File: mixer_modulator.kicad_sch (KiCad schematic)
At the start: 8 parts, among them U4 SA612, U5 SA612, U6 SA612, U7 SA612

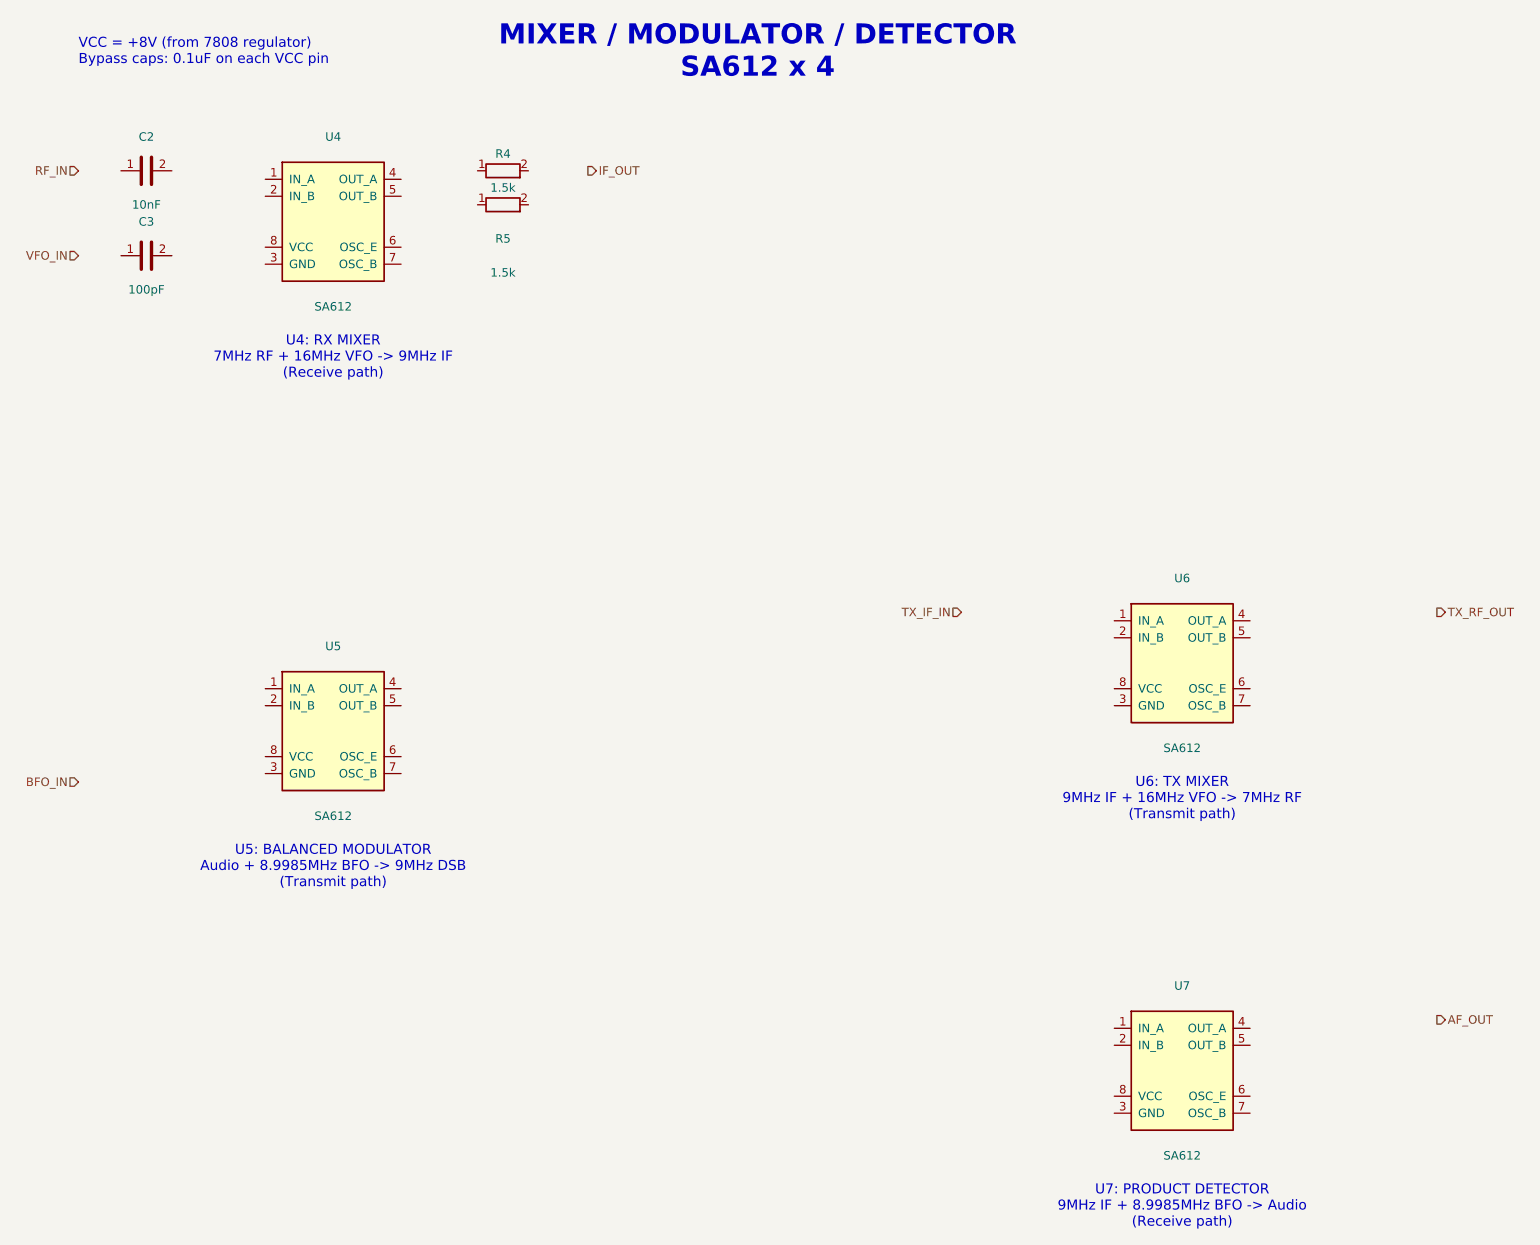
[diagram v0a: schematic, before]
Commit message: Add initial PCB layout with complete component placement
- Create 2-layer PCB (200x100mm) based on KiCad schematic import
- Place all components including Arduino Nano, Si5351, SA612 mixers, SSD1306 OLED
- Position audio amplifier (LM386), voltage regulators (7805/7808), crystal filters
- Add discrete components: resistors, capacitors, inductors, diodes, transistors
- Include connectors for power (DC jack), antenna, speaker, and microphone
- Update .gitignore to exclude fp-info-cache and backup directories
- Update schematic symbols for all circuit blocks (audio, BPF/LPF, control, IF filter, mixer/modulator, power amp, power supply)
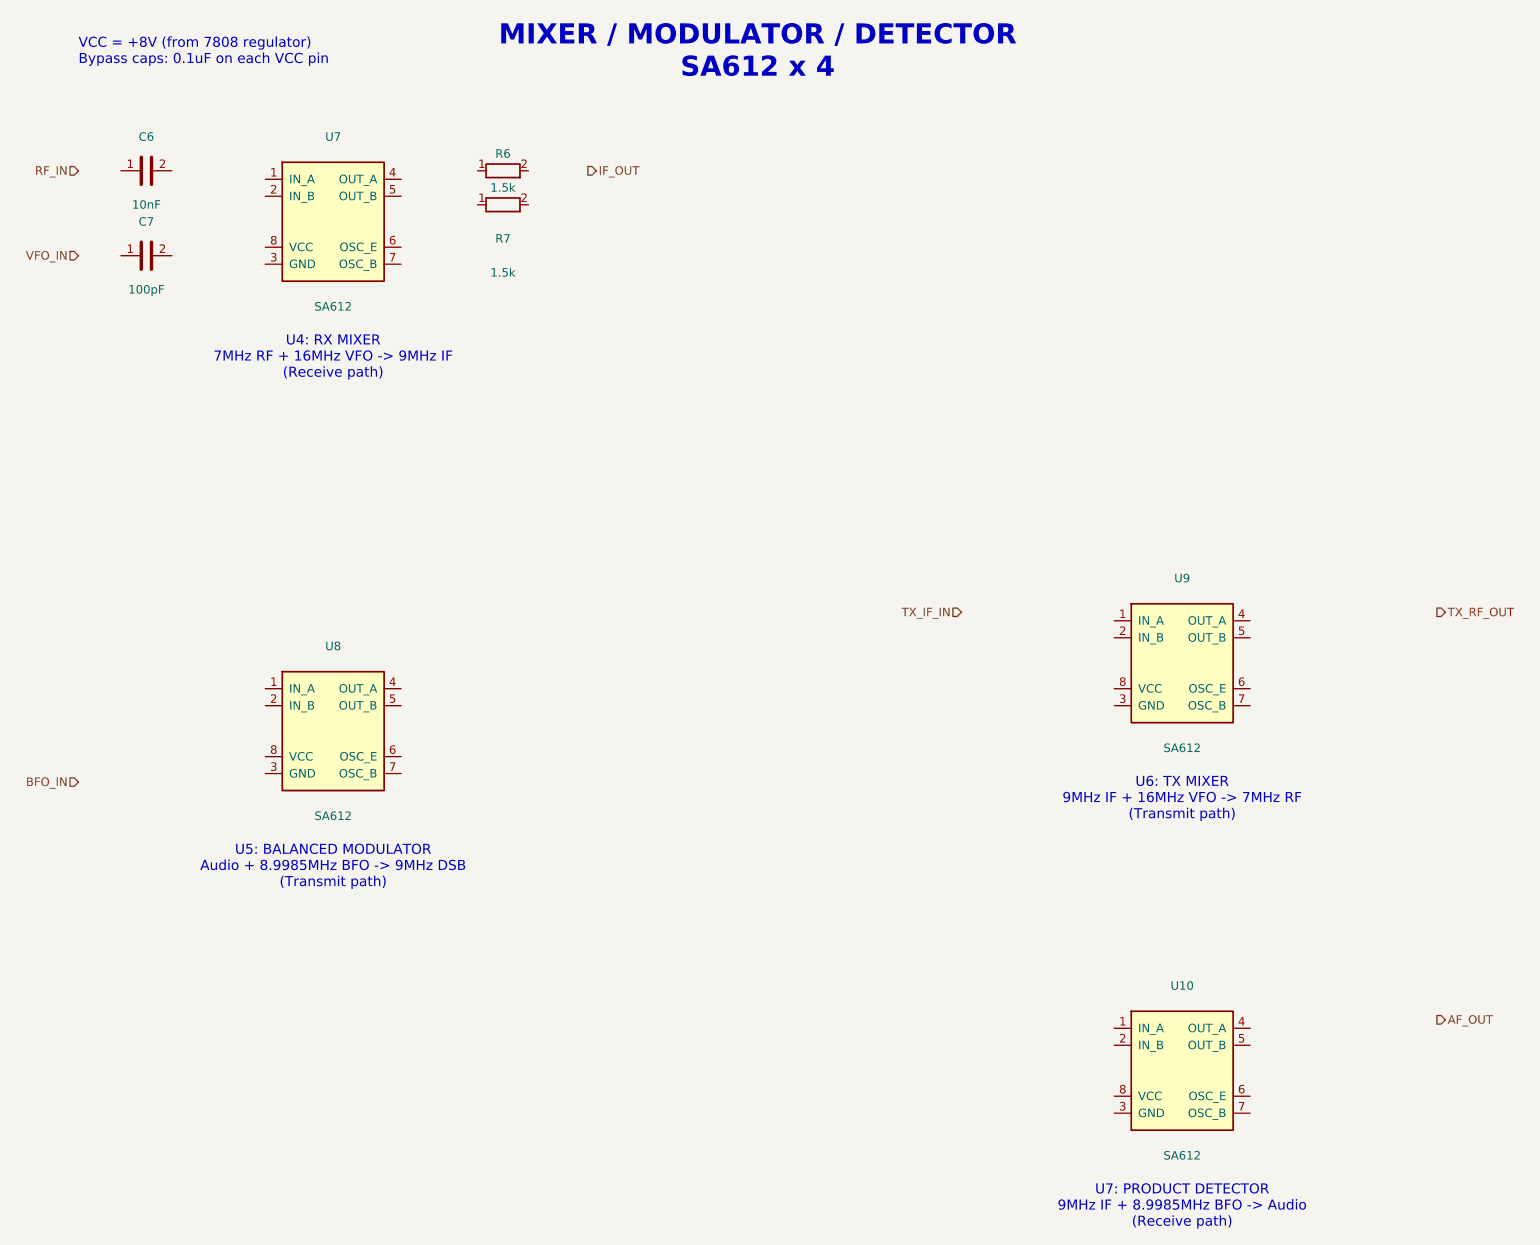
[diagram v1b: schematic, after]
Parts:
- removed C2: 10nF, symbol Device:C
- removed C3: 100pF, symbol Device:C
- removed R4, R5: 1.5k, symbol Device:R
- removed U4, U5, U6: SA612, symbol SA612:SA612
- added C6: 10nF, Capacitor_THT:C_Disc_D5.0mm_W2.5mm_P5.00mm, symbol Device:C
- added C7: 100pF, Capacitor_THT:C_Disc_D5.0mm_W2.5mm_P5.00mm, symbol Device:C
- added R6, R7: 1.5k, Resistor_THT:R_Axial_DIN0207_L6.3mm_D2.5mm_P10.16mm_Horizontal, symbol Device:R
- added U10, U8, U9: SA612, Package_DIP:DIP-8_W7.62mm, symbol SA612:SA612
- U7: footprint (none) -> Package_DIP:DIP-8_W7.62mm
